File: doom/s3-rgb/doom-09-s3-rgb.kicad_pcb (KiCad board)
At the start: 4 copper layers, 182 x 80 mm, 103 parts, among them J1 FH34SRJ-40S-0.5SH(50), J3 USB4105-GF-A, Q1 AO3401A, Q2 FS8205A, SW1 PTS645SM43SMTR92 LFS, SW10 PTS645SM43SMTR92 LFS, SW11 MSK12C02, SW12 PTS645SM43SMTR92 LFS, SW13 PTS645SM43SMTR92 LFS, SW2 PTS645SM43SMTR92 LFS, SW3 PTS645SM43SMTR92 LFS, SW4 PTS645SM43SMTR92 LFS, SW5 PTS645SM43SMTR92 LFS, SW6 PTS645SM43SMTR92 LFS, SW7 PTS645SM43SMTR92 LFS, SW8 PTS645SM43SMTR92 LFS, SW9 PTS645SM43SMTR92 LFS, U1 ESP32-S3-WROOM-1-N16R8, U2 DW01A, U3 MCP23017-E/SO, U4 PCM5102APWR, U5 PAM8403DR, U6 TLV75533PDBVR, U7 BQ24075RGTR, U8 MT3608, U9 USBLC6-2SC6

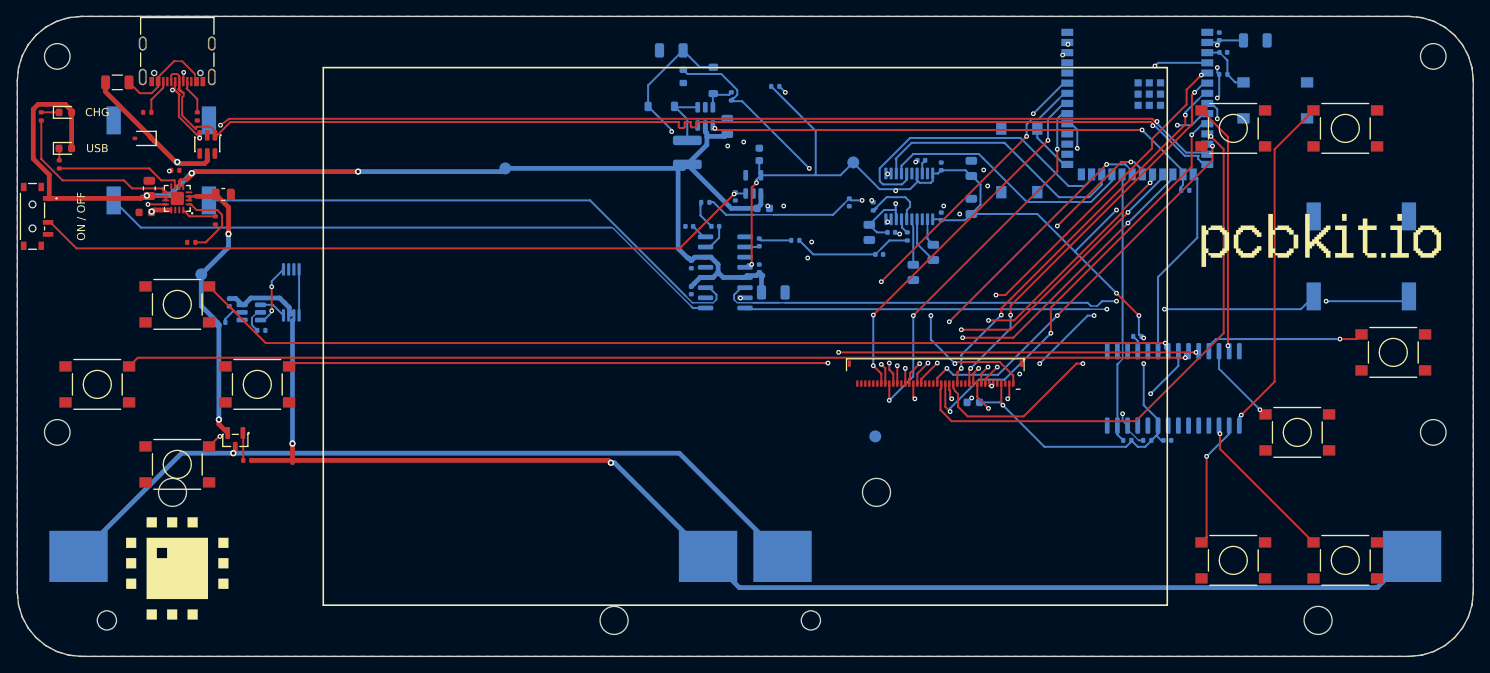
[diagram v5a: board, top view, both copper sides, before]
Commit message: Boards pass check and KiCad 10's DRC again: holes in courtyards, the USB net rename
pcbkit's check now has KiCad 10's pth/npth_inside_courtyard (pcbkit be5b6955), and 13 boards
failed it. KiCad's own DRC (kicad-cli 10) reports the same holes on every one of them.

- Parts that really stand above the holes under them (a screen or a Nano on its sockets, the
  Delta-S02's КМ-6 capacitors flat under its chips, as the factory placed them): a courtyard rule
  for the pair, written to each board's .kicad_dru, so KiCad's DRC agrees.
- Real collisions moved: servo-controller's dial 3 mm up (the Nano's socket pins came out under
  it), c3-pocket's fourth M3 hole from under a cell holder to the top edge's middle, s3-rgb's
  D-pad 2 mm up (a holder's peg came through under the down key).
- v003-emu, c3-pocket, rp2040-tft, rp2350-psram, s3-rgb, teensy41: re-routed for the standard USB
  block's renamed net (usb/raw is usb/vbusIn since pcbkit 2088839e): their tracks still carried
  the old name and shorted the fuse and connector pads.
- p4-touch-7: its board file still had a courtyard for the panel the design gives none (KiCad
  reported 114 courtyard errors); written again.

Measured on the dev host: all 44 registry boards `pcbkit check` complete with 0 errors, and
kicad-cli pcb drc 0 errors on every board.

Claude-Session: https://claude.ai/code/session_018URVYF1YPgyrMNetY9yT1T
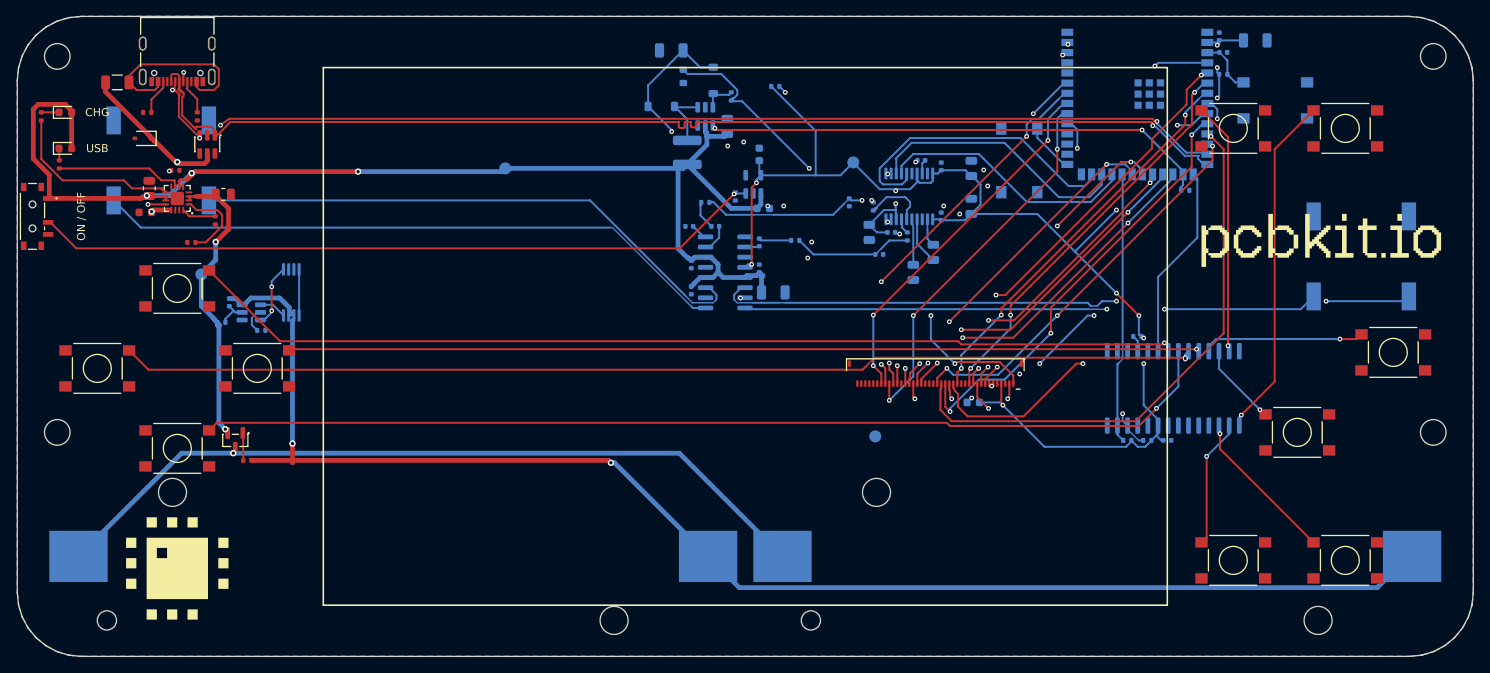
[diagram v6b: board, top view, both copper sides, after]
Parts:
- H1, H2, H3, H4: value (none) -> MountingHole_3.2mm_M3
- logo: value (none) -> Logo_PCBKit_pcbkit.io
- mark: value (none) -> Logo_PCBKit_mark
- tpBat, tpGnd, tpSys, tpV3: value (none) -> TestPoint_Round_D1.5mm
- wordmark: value (none) -> Logo_PCBKit_wordmark
- moved SW1 2.00 mm to (120.0, 154.0)
- moved SW2 2.00 mm to (120.0, 174.0)
- moved SW3 2.00 mm to (110.0, 164.0)
- moved SW4 2.00 mm to (130.0, 164.0)
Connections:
- net usb/power/raw renamed usb/power/vbusIn
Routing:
- net usb/power/vbusIn: track 12.9 -> 23.6 mm
- net RIGHT: track 117.3 -> 113.5 mm, vias 3 -> 1
- net UP: track 128.2 -> 124.6 mm
- net MENU: track 17.8 -> 16.0 mm
- net FIRE: track 22.0 -> 20.3 mm
- net KEYS_INT: track 25.8 -> 24.3 mm
- net STRAFE_R: track 44.3 -> 43.2 mm
- net DOWN: track 127.2 -> 128.2 mm, vias 2 -> 1
- net BL_FB: track 4.89 -> 4.21 mm
- net DAC_VNEG: track 7.01 -> 6.39 mm
- net LEFT: track 137.6 -> 136.9 mm, vias 1 -> 2
- net BAT: track 37.9 -> 37.3 mm

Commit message: doom: a resettable fuse per 18650 cell, a 2 % backlight clamp, a 1 A LDO on the S3 boards
The verifier (wiring-parallel-cells) found the two holders of every Doom board directly in parallel:
a cell put in backwards, or one much fuller than the other, drives the other through nothing but
the cells' resistance (about 56-168 A). Each holder's + now reaches BAT_IN through its own 2 A
resettable fuse (Littelfuse 1812L200/16GR, C18198340: 16 V, 100 A interrupting) on new nets
CELL1_P / CELL2_P. Nothing else moved; the boards were re-routed for the new nets.

- s3-rgb: the MT3608 backlight's open-panel clamp was a 28 V 5 % zener (bound 30.0 V against the
  switch's 30 V). It is now two 2 % zeners in series, UDZVTE-1718B + UDZVTE-1710B (27.33-28.56 V;
  LCSC stocks no single 28 V 2 % part). That is under 29.2 V and above the panel's 27.2 V.
- s3-rgb, s3-handheld: TLV75533 (500 mA) -> TLV75733 (1 A, C485517, same DBV pins; sheet from
  SBVS322C), for the ESP32-S3's 500 mA supply peaks (erc-supply-peak).
- c3-pocket, v003-emu: the USB PTC's hold is 750 mA, as the part (nSMD075) is (rating-current).
- pico2-carrier: the CHG/PG LEDs 1.5 mm further from the display's courtyard. rp2350-handheld:
  the logo off the LCD's courtyard and BT1's peg.
- READMEs: the per-cell fuses, the boards already ordered (s3-rgb, JLC W2026102705013253: insert
  the cells one at a time), status and BOM as check and the fab export give them now.

Measured on the dev host (pcbkit 5e0d2cc8): all 11 complete, 0 errors, 0 unrouted. What is left is
erc-rail-name (sent to the verifier as false positives) and full-speed USB pair coupling. The MCU
pins' nets are unchanged on every board, so the firmware and its simulation are unchanged.

Claude-Session: https://claude.ai/code/session_01B3VRfBCg9vAvGVWujVGarr
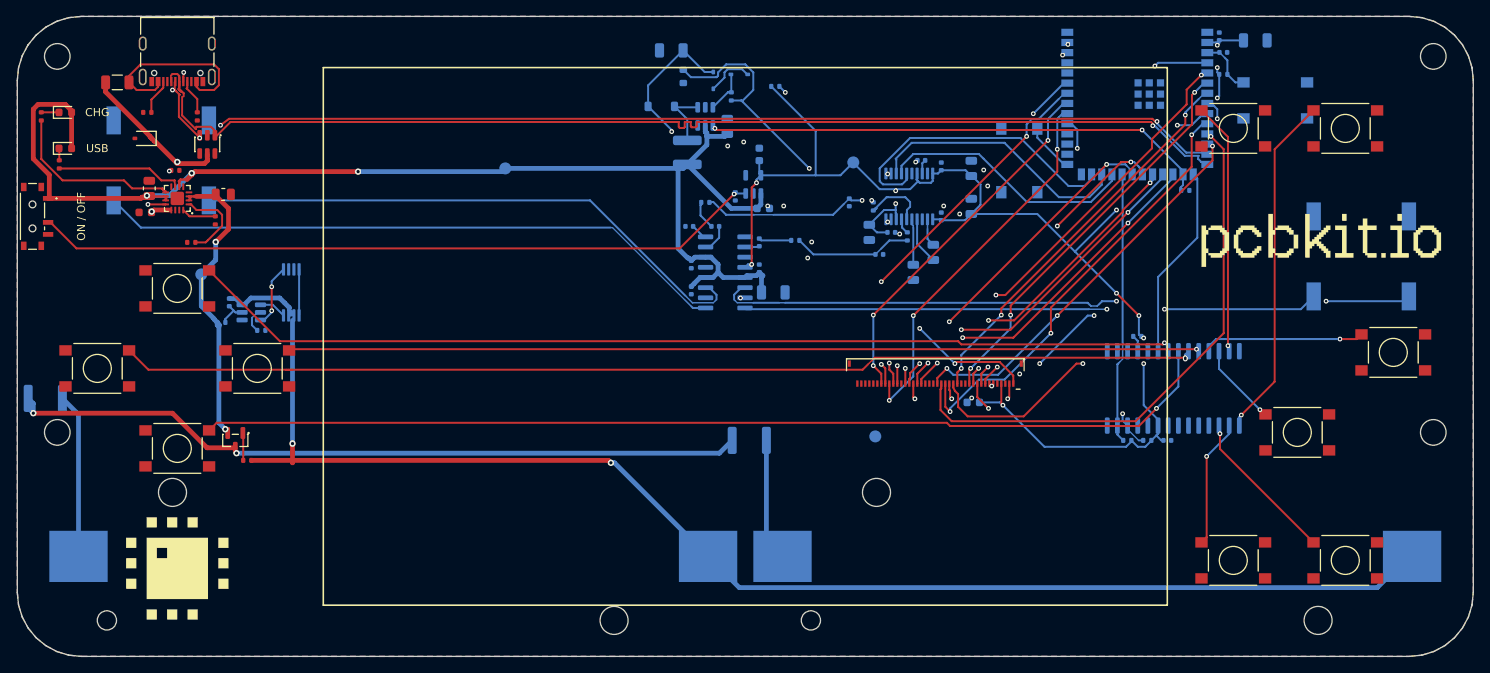
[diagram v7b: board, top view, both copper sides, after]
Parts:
- added D3: zener 10V, D_SOD-323, B.Cu at (190.2, 127.2)
- added F2: PTC 2000mA, Fuse_1812_4532Metric, B.Cu at (103.5, 167.8)
- added F3: PTC 2000mA, Fuse_1812_4532Metric, B.Cu at (191.5, 173.0)
- D2: value zener 28V -> zener 18V; footprint D_SOD-123 -> D_SOD-323
- U6: value TLV75533PDBVR -> TLV75733PDBVR
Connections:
- BT1 pad 2: BAT_IN -> CELL1_P
- BT2 pad 2: BAT_IN -> CELL2_P
- D2 pad 2: BL_FB -> BL_OVP
- SW1 pad 2: UP -> GND
- SW10 pad 2: ENTER -> GND
- SW12 pad 2: EN -> GND
- SW13 pad 2: Net-(SW13-1) -> GND
- SW2 pad 2: DOWN -> GND
- SW3 pad 2: LEFT -> GND
- SW4 pad 2: RIGHT -> GND
- SW5 pad 2: STRAFE_L -> GND
- SW6 pad 2: STRAFE_R -> GND
- SW7 pad 2: FIRE -> GND
- SW8 pad 2: USE -> GND
- SW9 pad 2: MENU -> GND
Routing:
- net CELL1_P: track 0.00 -> 20.6 mm
- net CELL2_P: track 0.00 -> 15.3 mm
- net BL_OVP: track 0.00 -> 5.96 mm
- net LED_K: track 63.8 -> 69.0 mm
- net BAT_IN: track 98.7 -> 93.9 mm, vias 1 -> 2
- net BL_FB: track 4.21 -> 5.34 mm

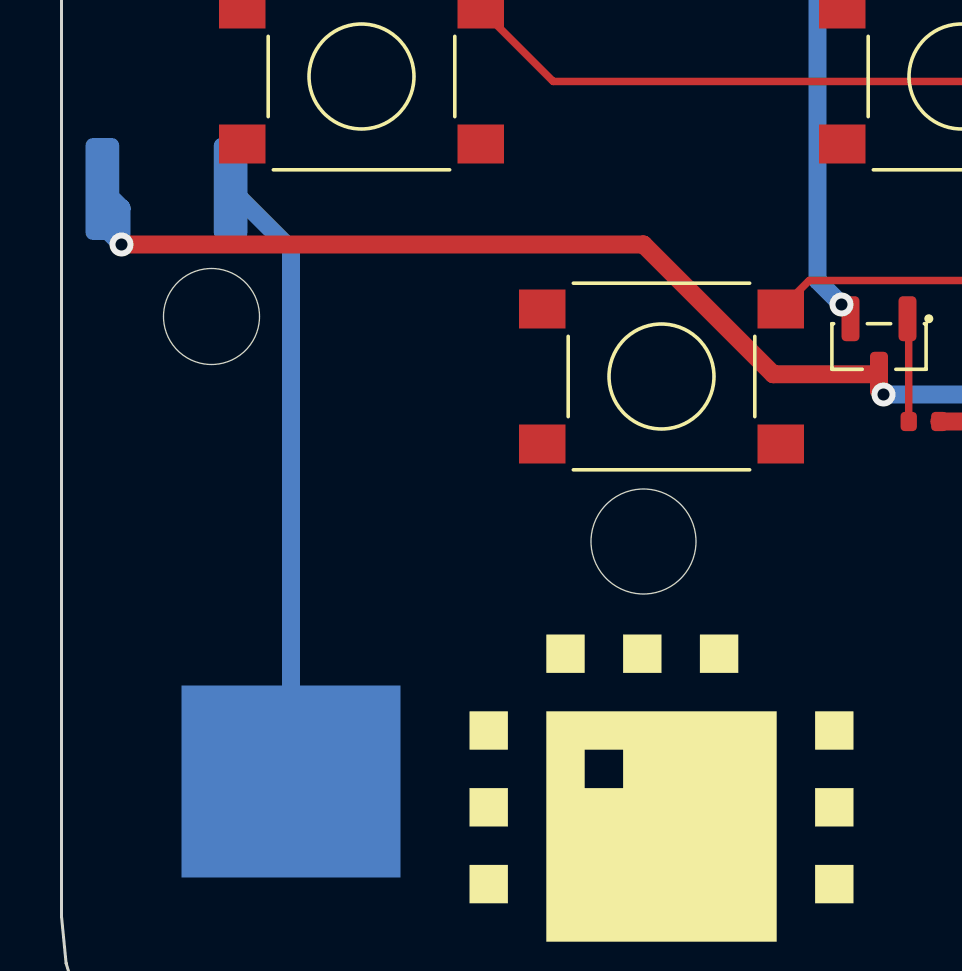
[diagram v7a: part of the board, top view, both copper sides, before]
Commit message: boards: 15 boards rebuilt on pcbkit 20ffacdc9 (their pours under the 0.25 mm hole clearance)
Every board checked with main: 17 of 44 failed on hole-clearance (pours filled before fill c6 made
0.25 mm KiCad's hole clearance the default), keepout (holes now sized by the board) or
place-corner. design.run {} on each (placement and routing kept, pours refilled): 15 now complete,
0 errors. Not here: esp32-p4-touch-lcd-7b and p4-touch-7 (a build reroutes their pairs: 21 and 7
unrouted; kept as they were, 2,372 and 919 hole-clearance errors: a refill without a reroute is
needed).

Claude-Session: https://claude.ai/code/session_01BAgp959tApA8aEg85EYgfb
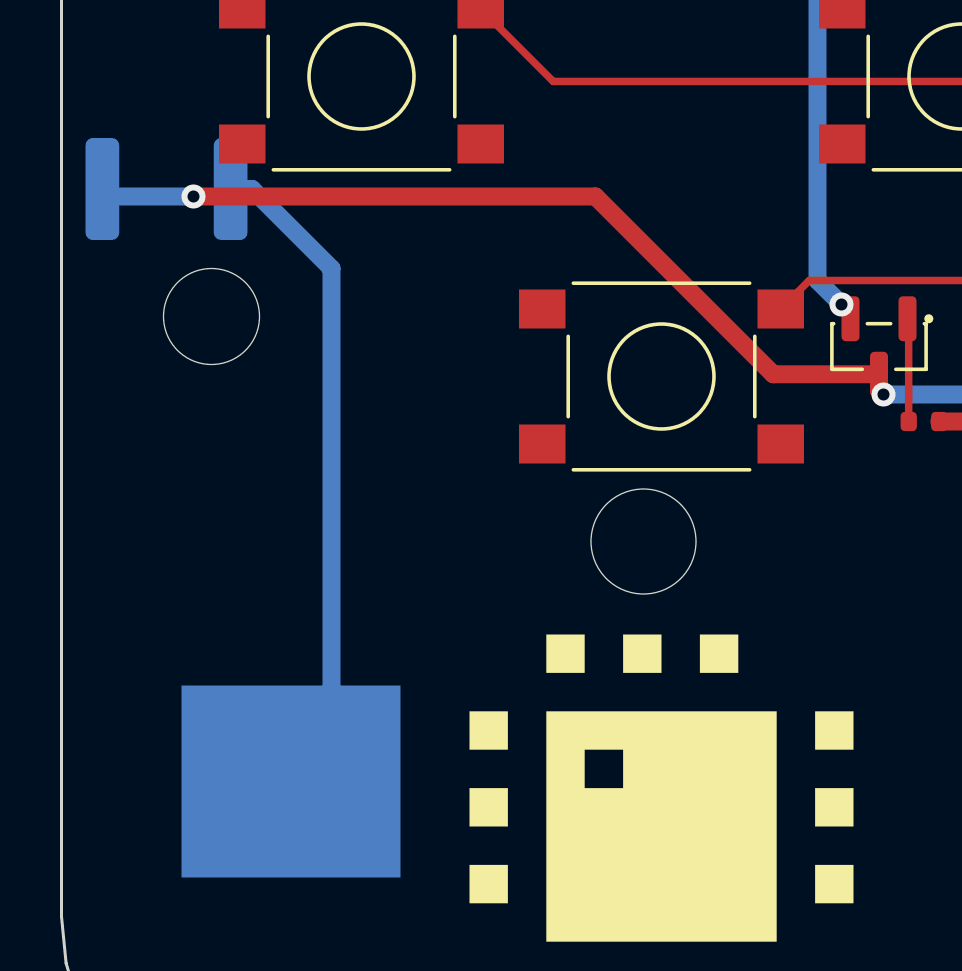
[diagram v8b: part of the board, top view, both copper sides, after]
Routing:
- net BAT_IN: track 93.9 -> 91.1 mm
- net CELL1_P: track 20.6 -> 22.1 mm
